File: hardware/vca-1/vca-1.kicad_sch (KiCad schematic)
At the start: 49 parts, among them J1 LIN CV IN, J2 AUDIO IN, J3 OUT, J4 LIN CV IN, J5 AUDIO IN, J6 OUT, J7 Conn_02x05_Odd_Even, Q1 BC557, Q2 BC557, U1 TL074, U2 LM13700

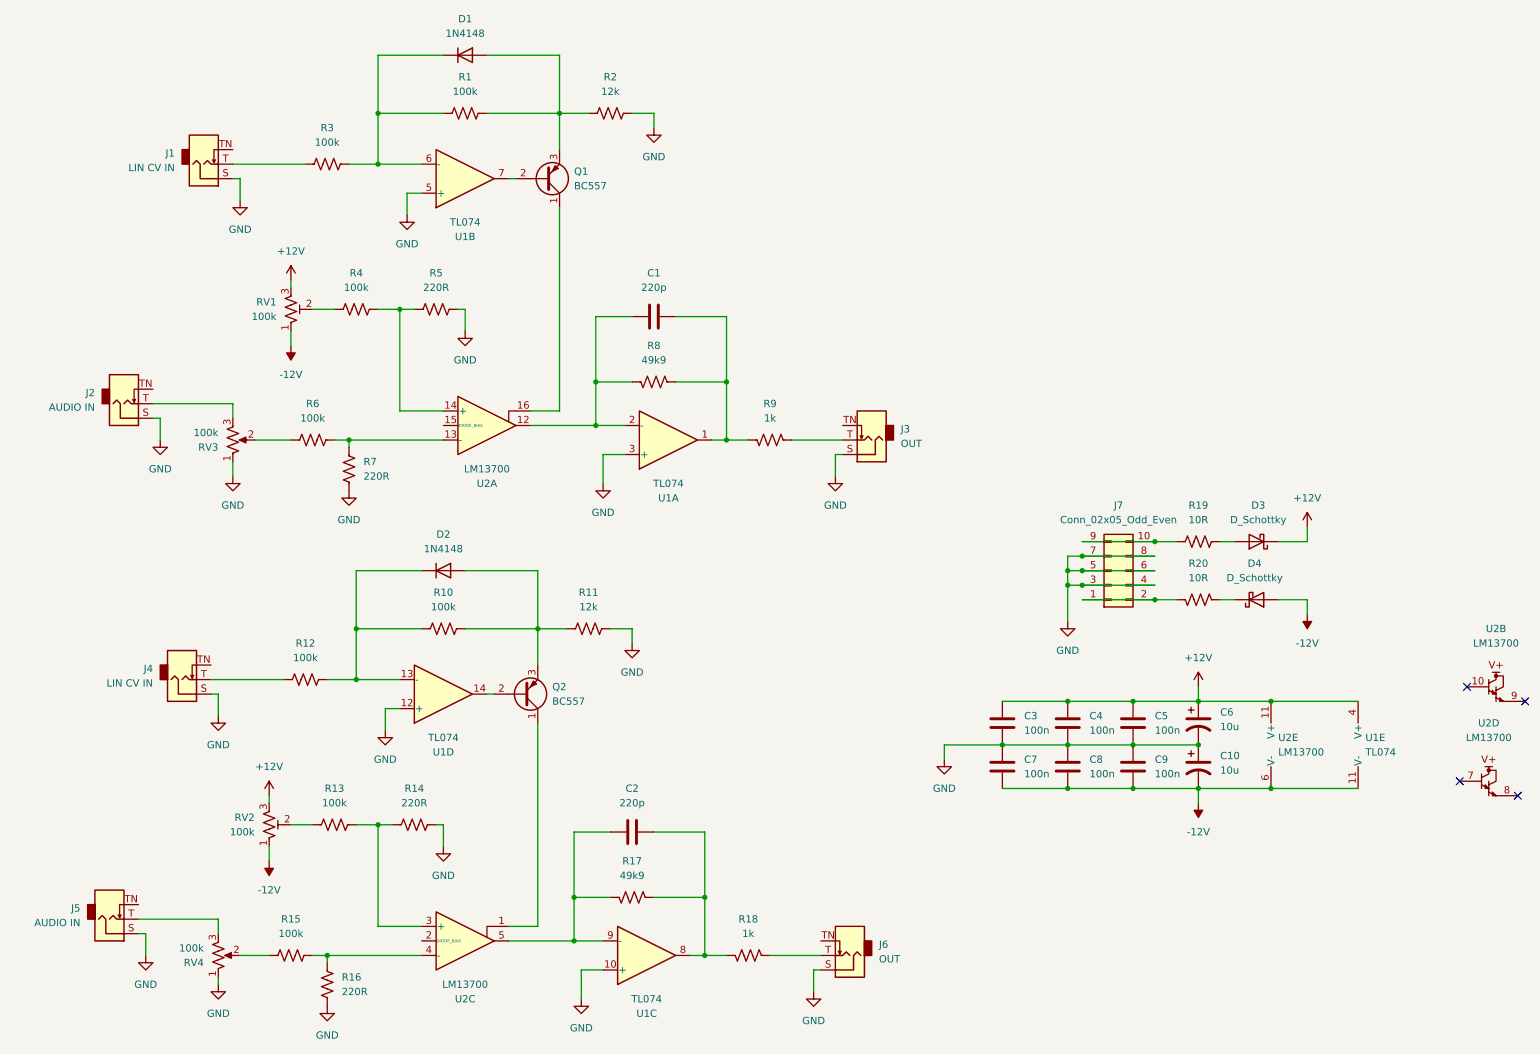
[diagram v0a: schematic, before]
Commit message: Updated component values for unity gain at 8V CV in to match ADSR
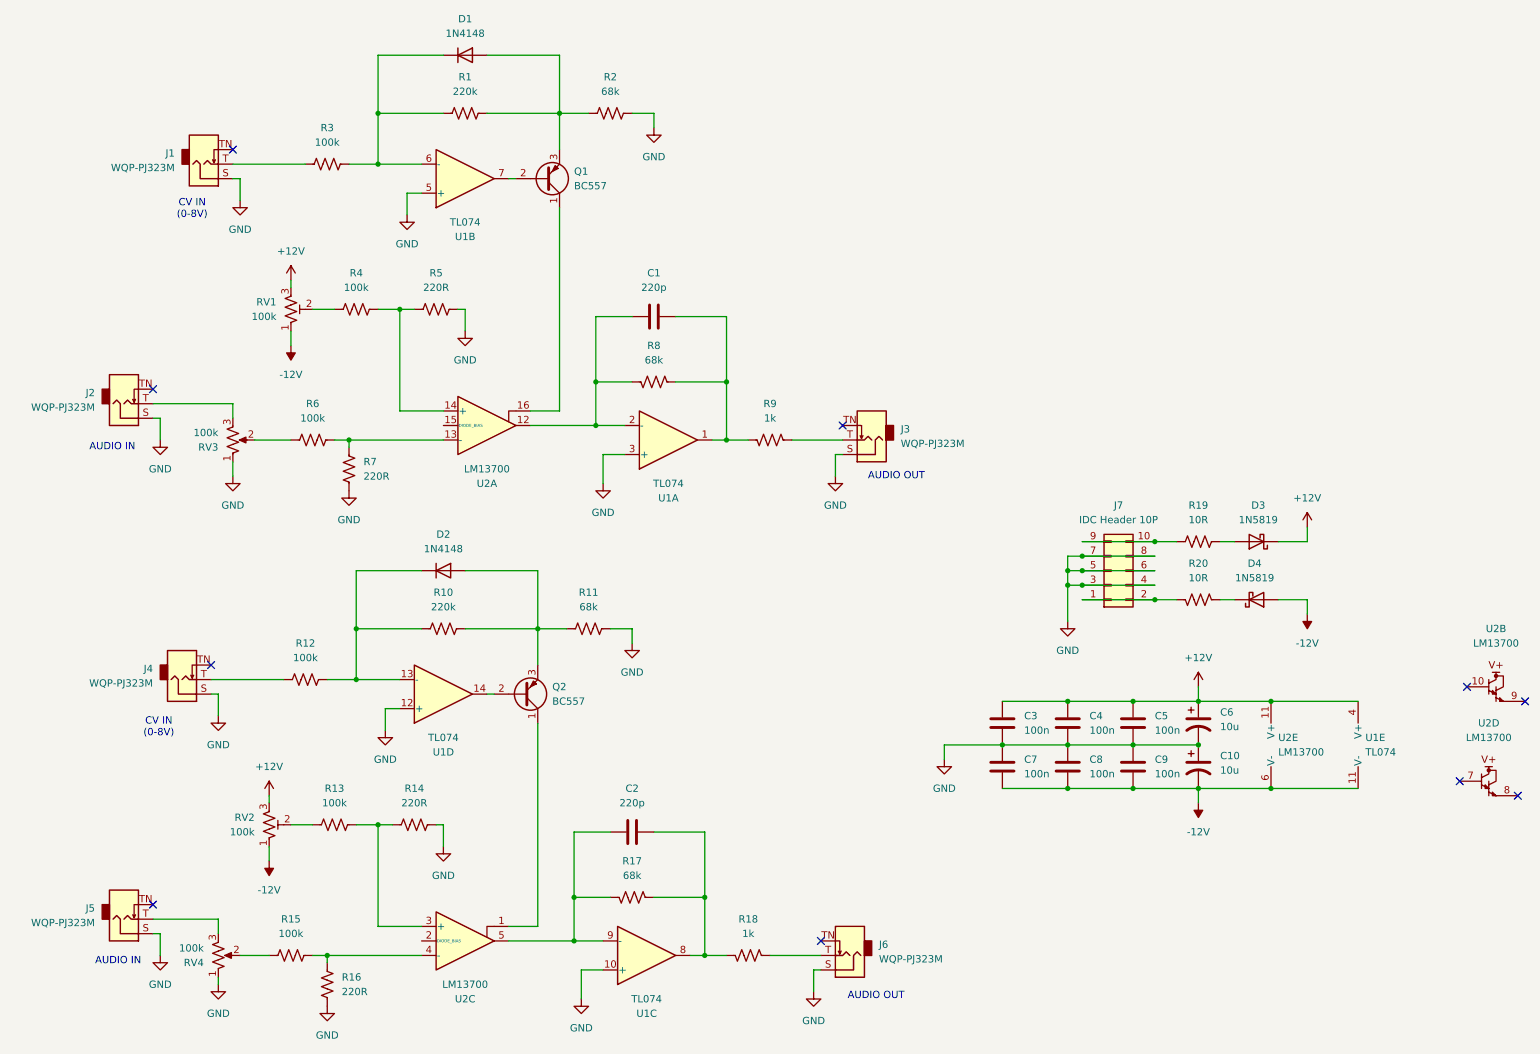
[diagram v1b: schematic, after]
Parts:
- D3, D4: value D_Schottky -> 1N5819
- J1, J4: value LIN CV IN -> WQP-PJ323M
- J2, J5: value AUDIO IN -> WQP-PJ323M
- J3, J6: value OUT -> WQP-PJ323M
- J7: value Conn_02x05_Odd_Even -> IDC Header 10P
- R1, R10: value 100k -> 220k
- R11, R2: value 12k -> 68k
- R17, R8: value 49k9 -> 68k
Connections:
- no-connect marks 4 -> 10
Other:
- note added: "AUDIO IN"
- note added: "AUDIO OUT"
- note added: "CV IN (0-8V)"
- moved on the sheet: J5
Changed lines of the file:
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@@
 	(title_block
 		(title "Dual VCA")
-		(date "2025-06-20")
+		(date "2025-10-31")
 		(rev "1.1")
 		(company "idyllm")
@@
 		(comment 2 "References: Aaron Lanterman, Thomas Henry")
 	)
+	(text "AUDIO IN"
+		(exclude_from_sim no)
+		(at 28.448 92.71 0)
+		(effects
+			(font
+				(size 1.27 1.27)
+			)
+		)
+	)
+	(text "AUDIO OUT"
+		(exclude_from_sim no)
+		(at 162.052 188.722 0)
+		(effects
+			(font
+				(size 1.27 1.27)
+			)
+		)
+	)
+	(text "AUDIO OUT"
+		(exclude_from_sim no)
+		(at 165.608 97.79 0)
+		(effects
+			(font
+				(size 1.27 1.27)
+			)
+		)
+	)
+	(text "CV IN\n(0-8V)"
+		(exclude_from_sim no)
+		(at 36.576 141.732 0)
+		(effects
+			(font
+				(size 1.27 1.27)
+			)
+		)
+	)
+	(text "CV IN\n(0-8V)"
+		(exclude_from_sim no)
+		(at 42.418 51.054 0)
+		(effects
+			(font
+				(size 1.27 1.27)
+			)
+		)
+	)
+	(text "AUDIO IN"
+		(exclude_from_sim no)
+		(at 29.464 182.626 0)
+		(effects
+			(font
+				(size 1.27 1.27)
+			)
+		)
+	)
 	(junction
 		(at 66.04 181.61)
@@
 	)
 	(no_connect
+		(at 152.4 179.07)
+	)
+	(no_connect
 		(at 265.43 134.62)
 	)
@@
 	)
 	(no_connect
+		(at 35.56 172.72)
+	)
+	(no_connect
+		(at 45.72 130.81)
+	)
+	(no_connect
 		(at 275.59 137.16)
 	)
 	(no_connect
+		(at 49.53 40.64)
+	)
+	(no_connect
+		(at 35.56 82.55)
+	)
+	(no_connect
+		(at 156.21 88.9)
+	)
+	(no_connect
 		(at 264.16 151.13)
 	)
@@
 	(wire
 		(pts
-			(xy 33.02 175.26) (xy 46.99 175.26)
+			(xy 35.56 175.26) (xy 46.99 175.26)
 		)
 		(stroke
@@
 	(wire
 		(pts
-			(xy 34.29 177.8) (xy 33.02 177.8)
+			(xy 36.83 177.8) (xy 35.56 177.8)
 		)
 		(stroke
@@
 	(wire
 		(pts
-			(xy 34.29 181.61) (xy 34.29 177.8)
+			(xy 36.83 181.61) (xy 36.83 177.8)
 		)
 		(stroke
@@
 	(symbol
 		(lib_id "Connector_Audio:AudioJack2_SwitchT")
-		(at 27.94 175.26 0)
+		(at 30.48 175.26 0)
 		(mirror x)
 		(unit 1)
@@
 		(on_board yes)
 		(dnp no)
-		(fields_autoplaced yes)
 		(property "Reference" "J5"
-			(at 22.86 173.3549 0)
+			(at 25.4 173.3549 0)
 			(effects
 				(font
@@
 			)
 		)
-		(property "Value" "AUDIO IN"
-			(at 22.86 175.8949 0)
+		(property "Value" "WQP-PJ323M"
+			(at 25.4 175.8949 0)
 			(effects
 				(font
@@
 		)
 		(property "Footprint" "AudioJacks:Jack_3.5mm_QingPu_WQP-PJ323M_Horizontal"
-			(at 27.94 175.26 0)
+			(at 30.48 175.26 0)
 			(effects
 				(font
@@
 		)
 		(property "Datasheet" "~"
-			(at 27.94 175.26 0)
+			(at 30.48 175.26 0)
 			(effects
 				(font
@@
 		)
 		(property "Description" "Audio Jack, 2 Poles (Mono / TS), Switched T Pole (Normalling)"
-			(at 27.94 175.26 0)
+			(at 30.48 175.26 0)
 			(effects
 				(font
@@
 			)
 		)
-		(property "Value" "49k9"
+		(property "Value" "68k"
 			(at 119.38 167.64 90)
 			(effects
@@
 			)
 		)
-		(property "Value" "49k9"
+		(property "Value" "68k"
 			(at 123.19 77.47 90)
 			(effects
@@
 			)
 		)
-		(property "Value" "LIN CV IN"
+		(property "Value" "WQP-PJ323M"
 			(at 39.37 43.8149 0)
 			(effects
@@
 			)
 		)
-		(property "Value" "LIN CV IN"
+		(property "Value" "WQP-PJ323M"
 			(at 35.56 133.9849 0)
 			(effects
@@
 			)
 		)
-		(property "Value" "12k"
+		(property "Value" "68k"
 			(at 115.57 30.48 90)
 			(effects
@@
 	(symbol
 		(lib_id "power:GND")
-		(at 34.29 181.61 0)
+		(at 36.83 181.61 0)
 		(unit 1)
 		(exclude_from_sim no)
@@
 		(fields_autoplaced yes)
 		(property "Reference" "#PWR017"
-			(at 34.29 187.96 0)
+			(at 36.83 187.96 0)
 			(effects
 				(font
@@
 		)
 		(property "Value" "GND"
-			(at 34.29 186.69 0)
+			(at 36.83 186.69 0)
 			(effects
 				(font
@@
 		)
 		(property "Footprint" ""
-			(at 34.29 181.61 0)
+			(at 36.83 181.61 0)
 			(effects
 				(font
@@
 		)
 		(property "Datasheet" ""
-			(at 34.29 181.61 0)
+			(at 36.83 181.61 0)
 			(effects
 				(font
@@
 		)
 		(property "Description" "Power symbol creates a global label with name \"GND\" , ground"
-			(at 34.29 181.61 0)
+			(at 36.83 181.61 0)
 			(effects
 				(font
@@
 			)
 		)
-		(property "Value" "100k"
+		(property "Value" "220k"
 			(at 90.17 30.48 90)
 			(effects
@@
 			)
 		)
-		(property "Value" "100k"
+		(property "Value" "220k"
 			(at 86.36 120.65 90)
 			(effects
@@
 			)
 		)
-		(property "Value" "D_Schottky"
+		(property "Value" "1N5819"
 			(at 228.9175 105.41 0)
 			(effects
@@
 			)
 		)
-		(property "Value" "D_Schottky"
+		(property "Value" "1N5819"
 			(at 228.2825 115.57 0)
 			(effects
@@
 			)
 		)
-		(property "Value" "OUT"
+		(property "Value" "WQP-PJ323M"
 			(at 162.56 182.2449 0)
 			(effects
@@
 			)
 		)
-		(property "Value" "OUT"
+		(property "Value" "WQP-PJ323M"
 			(at 166.37 92.0749 0)
 			(effects
@@
 			)
 		)
-		(property "Value" "Conn_02x05_Odd_Even"
+		(property "Value" "IDC Header 10P"
 			(at 204.47 105.41 0)
 			(effects
@@
 			)
 		)
-		(property "Value" "AUDIO IN"
+		(property "Value" "WQP-PJ323M"
 			(at 25.4 85.7249 0)
 			(effects
@@
 			)
 		)
-		(property "Value" "12k"
+		(property "Value" "68k"
 			(at 111.76 120.65 90)
 			(effects

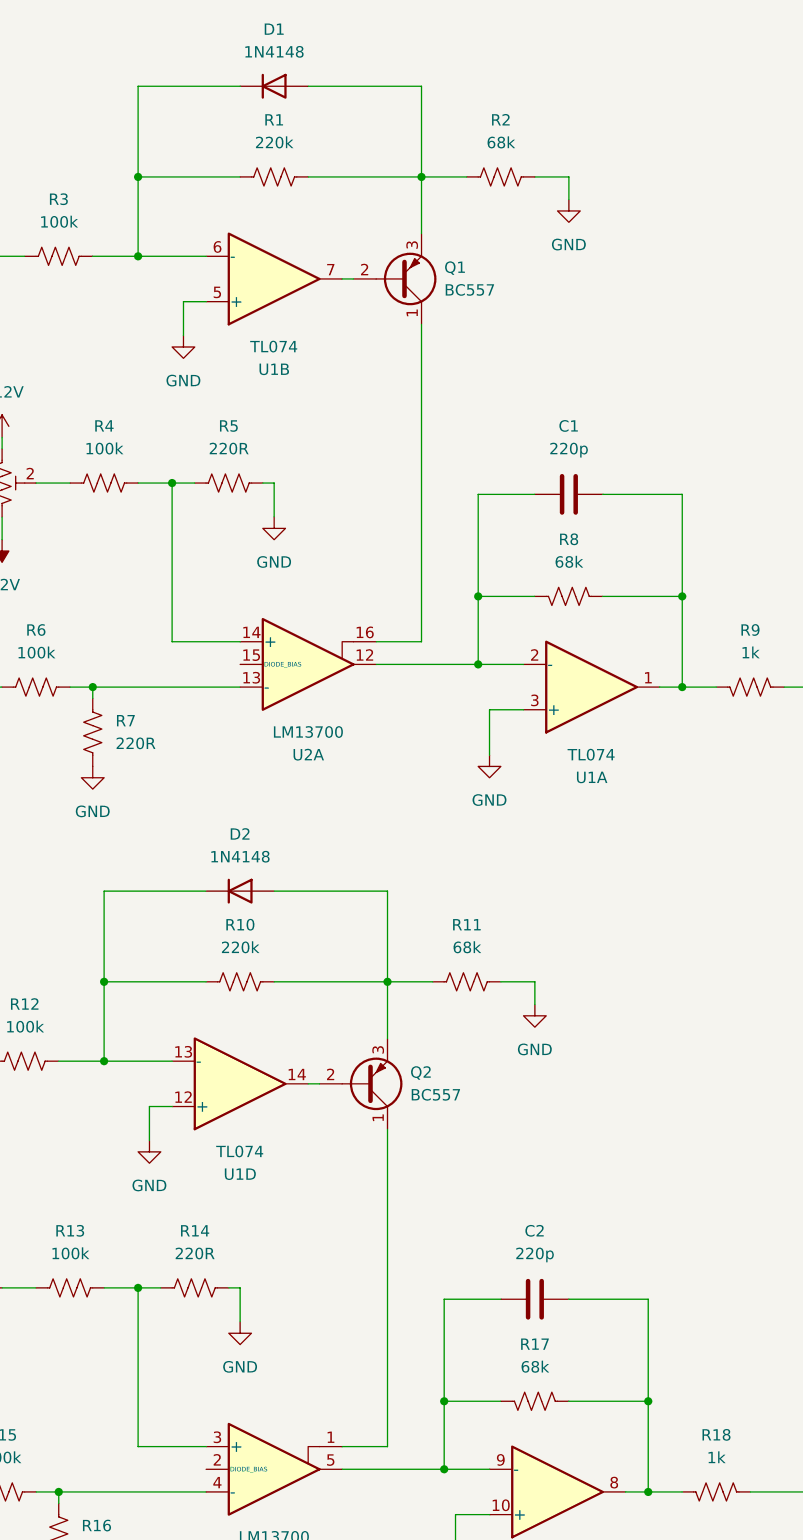
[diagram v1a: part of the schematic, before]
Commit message: Updated schematic values based on testing. Updated docs with measurements from board.
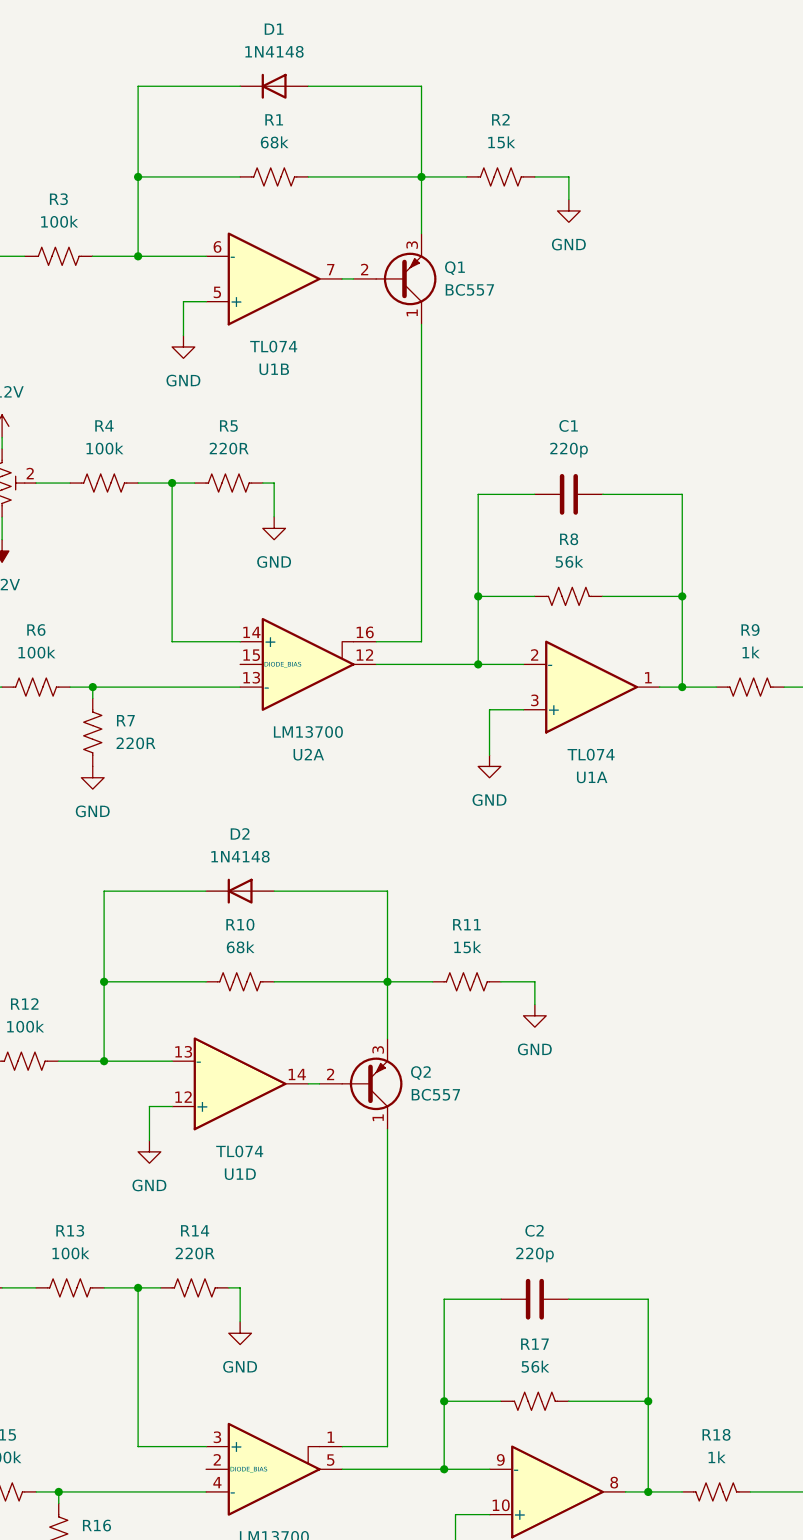
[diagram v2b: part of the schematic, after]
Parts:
- R1, R10: value 220k -> 68k
- R11, R2: value 68k -> 15k
- R17, R8: value 68k -> 56k
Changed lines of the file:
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@@
 	(title_block
 		(title "Dual VCA")
-		(date "2025-10-31")
-		(rev "1.1")
+		(date "2025-11-04")
+		(rev "1.2")
 		(company "idyllm")
 		(comment 1 "CC BY-SA 4.0")
@@
 			)
 		)
-		(property "Value" "68k"
+		(property "Value" "56k"
 			(at 119.38 167.64 90)
 			(effects
@@
 			)
 		)
-		(property "Value" "68k"
+		(property "Value" "56k"
 			(at 123.19 77.47 90)
 			(effects
@@
 			)
 		)
-		(property "Value" "68k"
+		(property "Value" "15k"
 			(at 115.57 30.48 90)
 			(effects
@@
 			)
 		)
-		(property "Value" "220k"
+		(property "Value" "68k"
 			(at 90.17 30.48 90)
 			(effects
@@
 			)
 		)
-		(property "Value" "220k"
+		(property "Value" "68k"
 			(at 86.36 120.65 90)
 			(effects
@@
 			)
 		)
-		(property "Value" "68k"
+		(property "Value" "15k"
 			(at 111.76 120.65 90)
 			(effects
